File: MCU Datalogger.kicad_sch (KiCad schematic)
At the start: 25 parts, among them U1 DS1337S+, U2 24LC1025, U3 24LC1025, U4 ATMEGA328P-AU, Y1 Crystal, Y2 Crystal

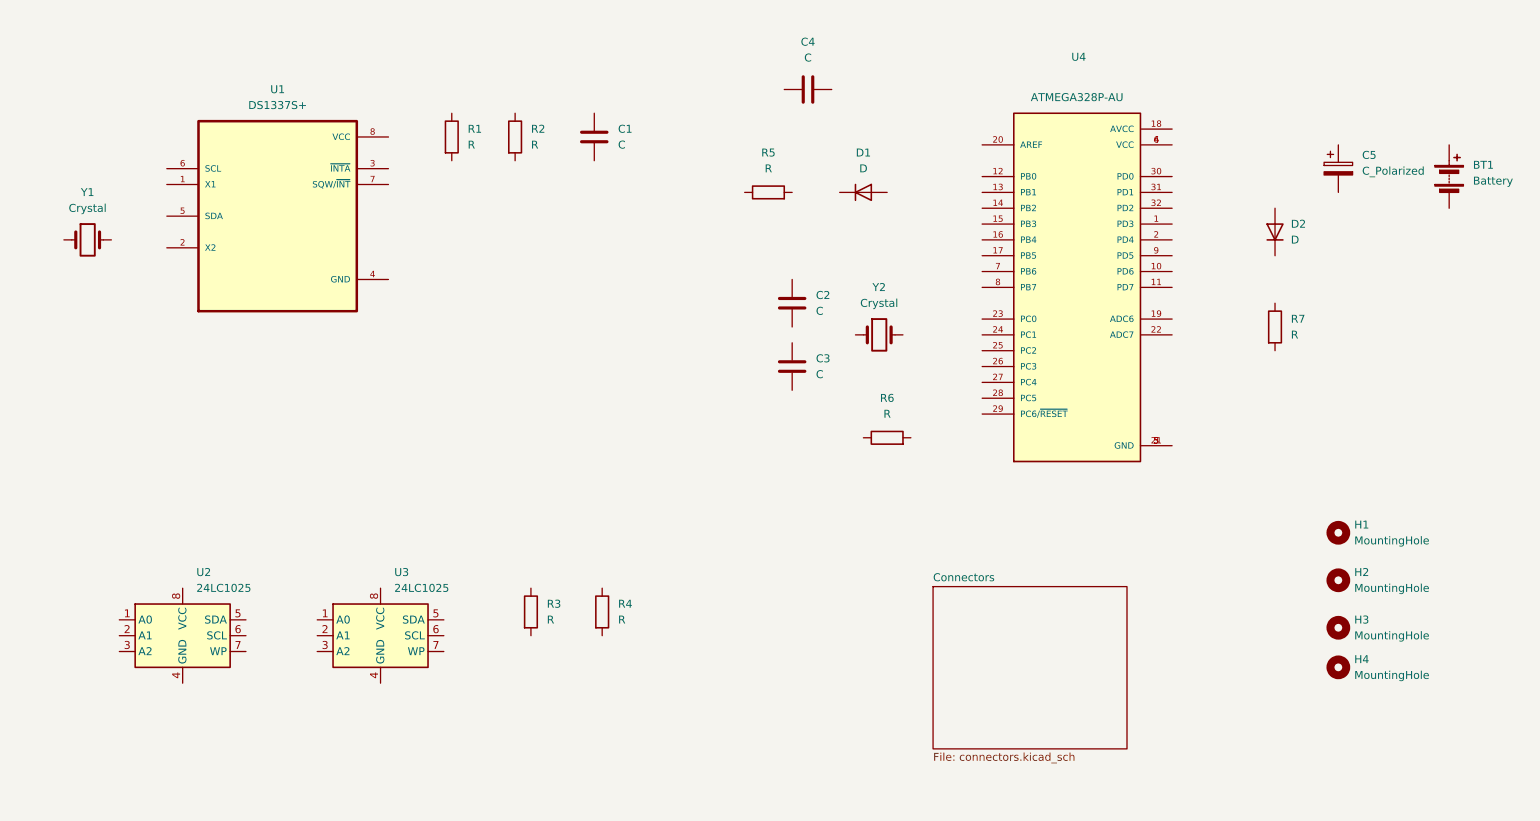
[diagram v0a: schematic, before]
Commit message: Added component values.
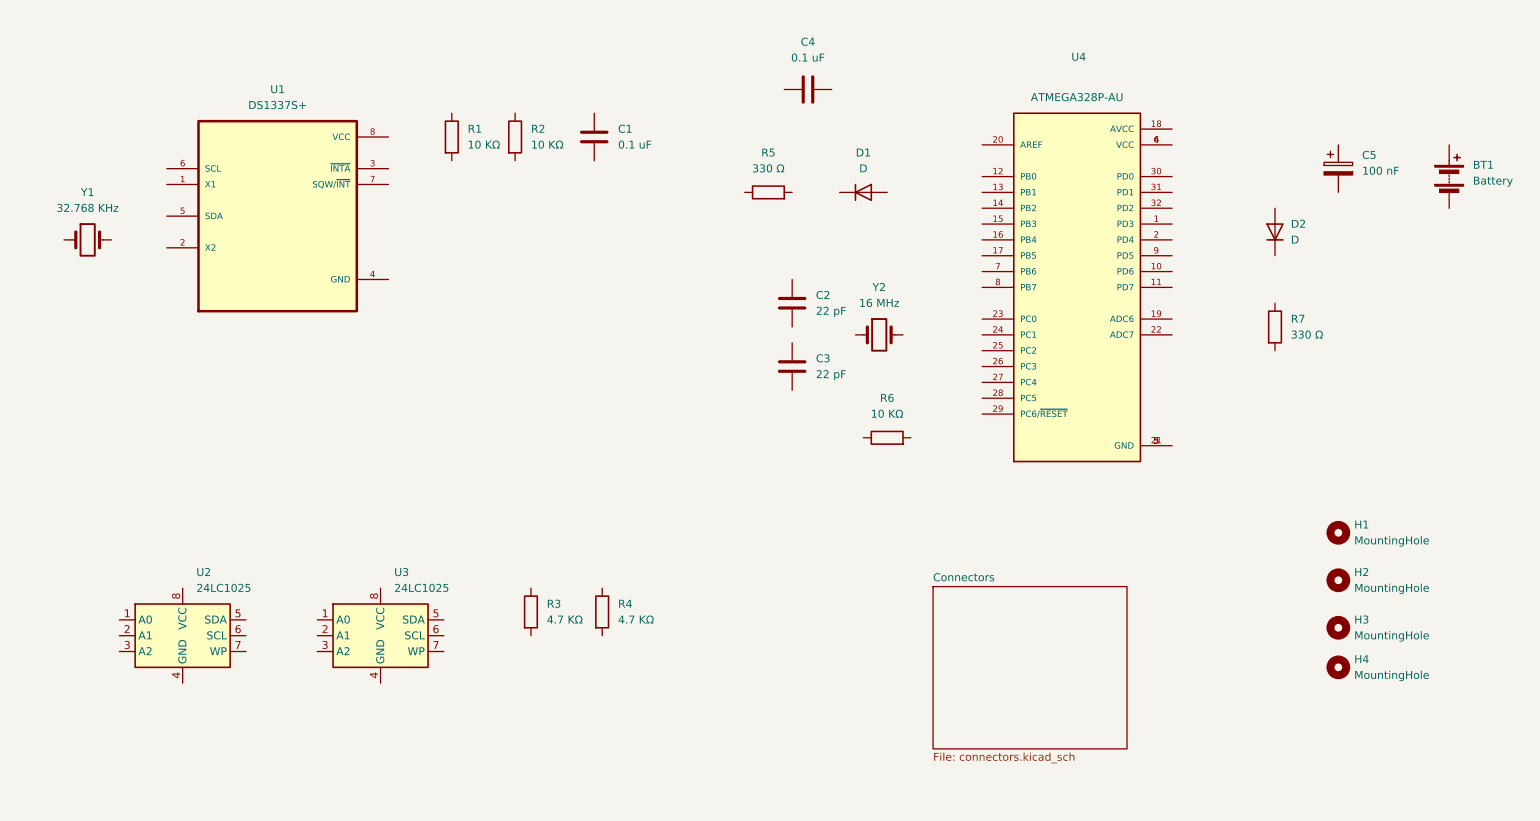
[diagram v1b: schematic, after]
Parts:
- C1, C4: value C -> 0.1 uF
- C2, C3: value C -> 22 pF
- C5: value C_Polarized -> 100 nF
- R1, R2, R6: value R -> 10 ΚΩ
- R3, R4: value R -> 4.7 ΚΩ
- R5, R7: value R -> 330 Ω
- Y1: value Crystal -> 32.768 KHz
- Y2: value Crystal -> 16 MHz
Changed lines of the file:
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@@
 			)
 		)
-		(property "Value" "C"
+		(property "Value" "0.1 uF"
 			(at 146.05 30.48 90)
 			(effects
@@
 			)
 		)
-		(property "Value" "C"
+		(property "Value" "22 pF"
 			(at 147.32 71.1199 0)
 			(effects
@@
 			)
 		)
+		(property "Purpose" ""
+			(at 143.51 69.85 0)
+			(effects
+				(font
+					(size 1.27 1.27)
+				)
+			)
+		)
 		(pin "2"
 		)
@@
 			)
 		)
-		(property "Value" "R"
+		(property "Value" "10 ΚΩ"
 			(at 158.75 87.63 90)
 			(effects
@@
 			)
 		)
-		(property "Value" "C"
+		(property "Value" "0.1 uF"
 			(at 115.57 44.4499 0)
 			(effects
@@
 			)
 		)
-		(property "Value" "R"
+		(property "Value" "10 ΚΩ"
 			(at 101.6 44.4499 0)
 			(effects
@@
 			)
 		)
-		(property "Value" "R"
+		(property "Value" "4.7 ΚΩ"
 			(at 104.14 120.6499 0)
 			(effects
@@
 			)
 		)
-		(property "Value" "R"
+		(property "Value" "10 ΚΩ"
 			(at 91.44 44.4499 0)
 			(effects
@@
 			)
 		)
-		(property "Value" "R"
+		(property "Value" "4.7 ΚΩ"
 			(at 115.57 120.6499 0)
 			(effects
@@
 			)
 		)
-		(property "Value" "Crystal"
+		(property "Value" "32.768 KHz"
 			(at 30.48 54.61 0)
 			(effects
@@
 			)
 		)
-		(property "Value" "Crystal"
+		(property "Value" "16 MHz"
 			(at 157.48 69.85 0)
 			(effects
@@
 			)
 		)
-		(property "Value" "C_Polarized"
+		(property "Value" "100 nF"
 			(at 234.95 48.6409 0)
 			(effects
@@
 			)
 		)
-		(property "Value" "R"
+		(property "Value" "330 Ω"
 			(at 139.7 48.26 90)
 			(effects
@@
 			)
 		)
-		(property "Value" "R"
+		(property "Value" "330 Ω"
 			(at 223.52 74.9299 0)
 			(effects
@@
 			)
 		)
-		(property "Value" "C"
+		(property "Value" "22 pF"
 			(at 147.32 81.2799 0)
 			(effects

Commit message: Completed symbol—footprint associations.
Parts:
- BT1: footprint (none) -> Connector_PinHeader_2.54mm:PinHeader_1x02_P2.54mm_Vertical
- C1, C2, C3, C4, C5: footprint (none) -> Capacitor_SMD:C_0805_2012Metric
- D1, D2: footprint (none) -> LED_SMD:LED_0805_2012Metric
- H1, H2, H3, H4: footprint (none) -> MountingHole:MountingHole_2.1mm
- R1, R2, R3, R4, R5, R6, R7: footprint (none) -> Resistor_SMD:R_0805_2012Metric
- U1: footprint SOIC127P600X175-8N -> Footprints:SOIC127P600X175-8N
- U2, U3: footprint (none) -> Package_SO:SOIC-8_5.23x5.23mm_P1.27mm
- U4: footprint QFP80P900X900X120-32N -> Footprints:QFP80P900X900X120-32N
- Y1, Y2: footprint (none) -> Crystal:Crystal_SMD_5032-2Pin_5.0x3.2mm_HandSoldering
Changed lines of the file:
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@@
 			)
 		)
-		(property "Footprint" ""
+		(property "Footprint" "Capacitor_SMD:C_0805_2012Metric"
 			(at 149.86 34.5948 0)
 			(effects
@@
 			)
 		)
-		(property "Footprint" ""
+		(property "Footprint" "Capacitor_SMD:C_0805_2012Metric"
 			(at 144.4752 73.66 0)
 			(effects
@@
 			)
 		)
-		(property "Footprint" ""
+		(property "Footprint" "Resistor_SMD:R_0805_2012Metric"
 			(at 158.75 93.218 90)
 			(effects
@@
 			)
 		)
-		(property "Footprint" ""
+		(property "Footprint" "Capacitor_SMD:C_0805_2012Metric"
 			(at 112.7252 46.99 0)
 			(effects
@@
 			)
 		)
-		(property "Footprint" ""
+		(property "Footprint" "LED_SMD:LED_0805_2012Metric"
 			(at 220.98 58.42 0)
 			(effects
@@
 			)
 		)
-		(property "Footprint" ""
+		(property "Footprint" "Resistor_SMD:R_0805_2012Metric"
 			(at 97.282 43.18 90)
 			(effects
@@
 			)
 		)
-		(property "Footprint" ""
+		(property "Footprint" "Resistor_SMD:R_0805_2012Metric"
 			(at 99.822 119.38 90)
 			(effects
@@
 			)
 		)
-		(property "Footprint" ""
+		(property "Footprint" "Resistor_SMD:R_0805_2012Metric"
 			(at 87.122 43.18 90)
 			(effects
@@
 			)
 		)
-		(property "Footprint" ""
+		(property "Footprint" "Connector_PinHeader_2.54mm:PinHeader_1x02_P2.54mm_Vertical"
 			(at 248.92 48.006 90)
 			(effects
@@
 			)
 		)
-		(property "Footprint" ""
+		(property "Footprint" "Resistor_SMD:R_0805_2012Metric"
 			(at 111.252 119.38 90)
 			(effects
@@
 			)
 		)
-		(property "Footprint" "QFP80P900X900X120-32N"
+		(property "Footprint" "Footprints:QFP80P900X900X120-32N"
 			(at 189.23 67.31 0)
 			(effects
@@
 			)
 		)
-		(property "Footprint" ""
+		(property "Footprint" "MountingHole:MountingHole_2.1mm"
 			(at 231.14 121.92 0)
 			(effects
@@
 			)
 		)
-		(property "Footprint" ""
+		(property "Footprint" "Crystal:Crystal_SMD_5032-2Pin_5.0x3.2mm_HandSoldering"
 			(at 30.48 59.69 0)
 			(effects
@@
 			)
 		)
-		(property "Footprint" ""
+		(property "Footprint" "MountingHole:MountingHole_2.1mm"
 			(at 231.14 106.68 0)
 			(effects
@@
 			)
 		)
-		(property "Footprint" ""
+		(property "Footprint" "Package_SO:SOIC-8_5.23x5.23mm_P1.27mm"
 			(at 77.47 123.19 0)
 			(effects
@@
 			)
 		)
-		(property "Footprint" "SOIC127P600X175-8N"
+		(property "Footprint" "Footprints:SOIC127P600X175-8N"
 			(at 60.96 55.88 0)
 			(effects
@@
 			)
 		)
-		(property "Footprint" ""
+		(property "Footprint" "MountingHole:MountingHole_2.1mm"
 			(at 231.14 114.3 0)
 			(effects
@@
 			)
 		)
-		(property "Footprint" ""
+		(property "Footprint" "Package_SO:SOIC-8_5.23x5.23mm_P1.27mm"
 			(at 45.72 123.19 0)
 			(effects
@@
 			)
 		)
-		(property "Footprint" ""
+		(property "Footprint" "LED_SMD:LED_0805_2012Metric"
 			(at 154.94 52.07 0)
 			(effects
@@
 			)
 		)
-		(property "Footprint" ""
+		(property "Footprint" "MountingHole:MountingHole_2.1mm"
 			(at 231.14 128.27 0)
 			(effects
@@
 			)
 		)
-		(property "Footprint" ""
+		(property "Footprint" "Crystal:Crystal_SMD_5032-2Pin_5.0x3.2mm_HandSoldering"
 			(at 157.48 74.93 0)
 			(effects
@@
 			)
 		)
-		(property "Footprint" ""
+		(property "Footprint" "Capacitor_SMD:C_0805_2012Metric"
 			(at 232.1052 52.07 0)
 			(effects
@@
 			)
 		)
-		(property "Footprint" ""
+		(property "Footprint" "Resistor_SMD:R_0805_2012Metric"
 			(at 139.7 53.848 90)
 			(effects
@@
 			)
 		)
-		(property "Footprint" ""
+		(property "Footprint" "Resistor_SMD:R_0805_2012Metric"
 			(at 219.202 73.66 90)
 			(effects
@@
 			)
 		)
-		(property "Footprint" ""
+		(property "Footprint" "Capacitor_SMD:C_0805_2012Metric"
 			(at 144.4752 83.82 0)
 			(effects

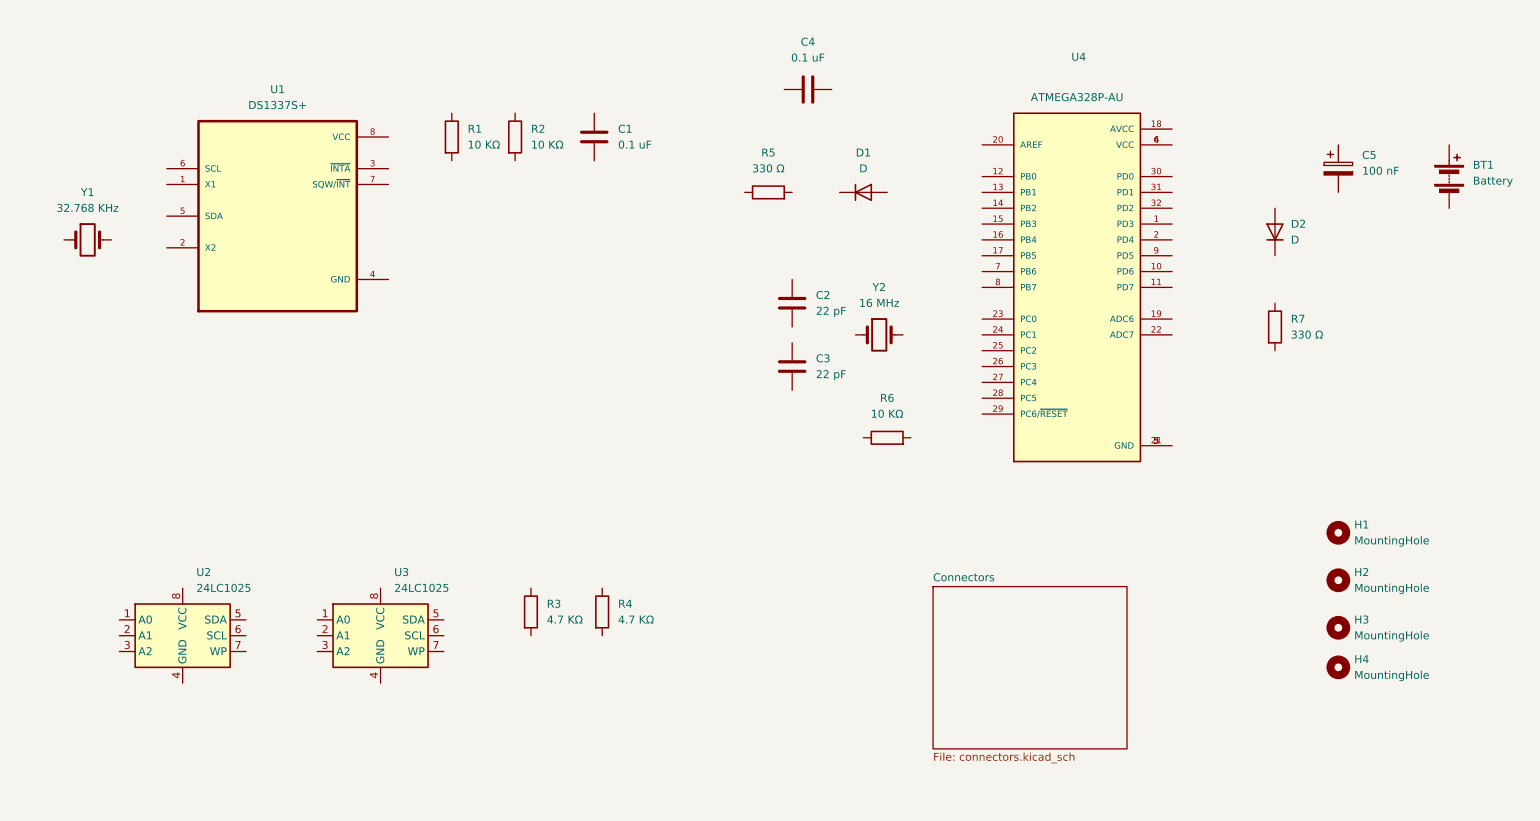
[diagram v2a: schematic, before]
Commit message: Completed wiring of main sheet.
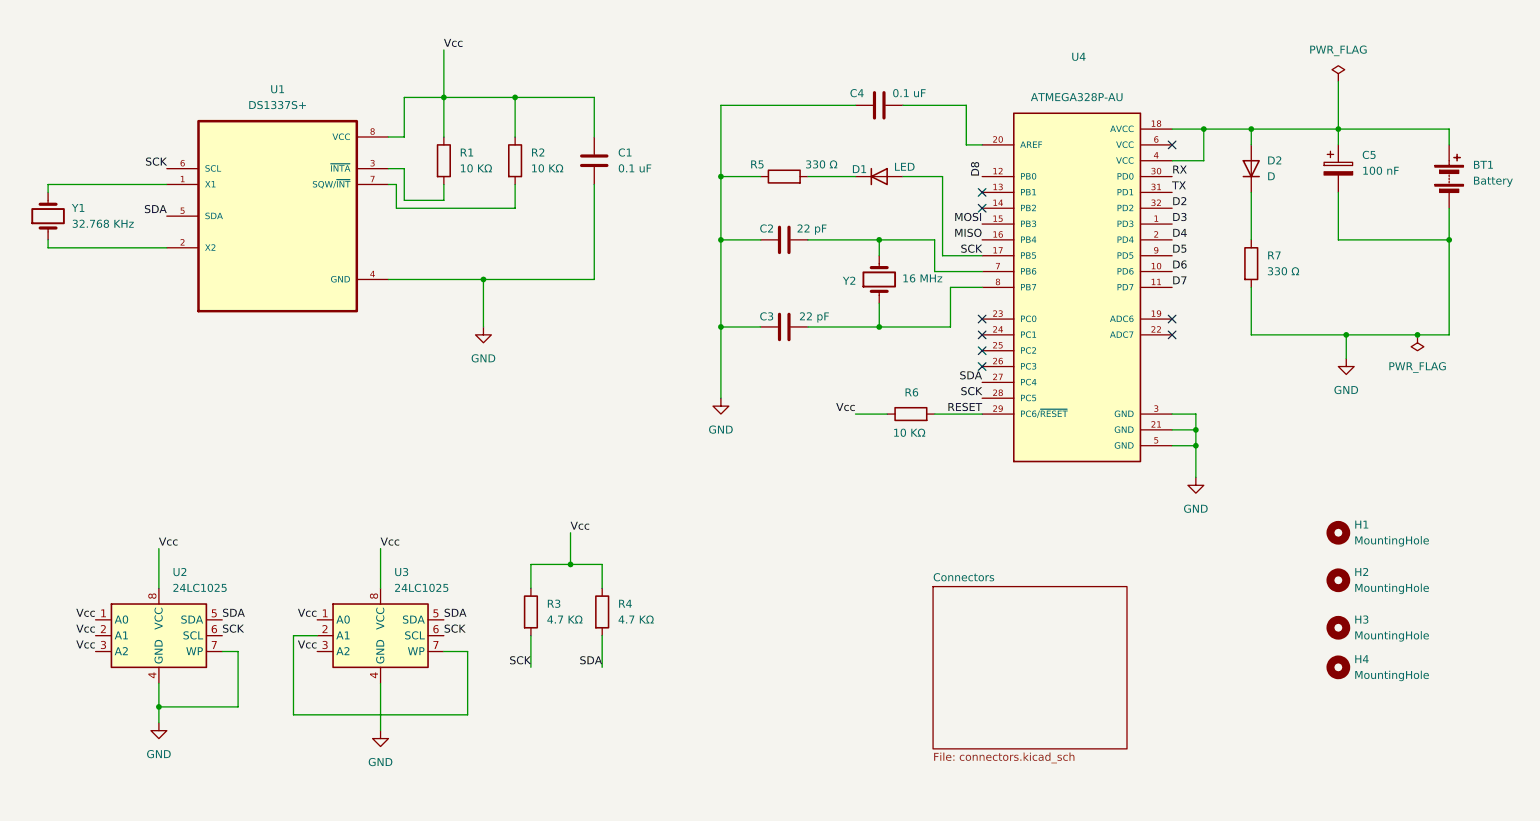
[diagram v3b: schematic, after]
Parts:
- D1: value D -> LED
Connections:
- net GND: now reaches C4.1
- net GND: now also BT1.2 (-), C1.2, C2.2, C3.1, C5.2, R5.1, R7.2, U1.4 (GND), U2.4 (GND), U2.7 (WP), U3.4 (GND), U4.21 (GND), U4.3 (GND), U4.5 (GND)
- net at C4.2: now also U4.20 (AREF)
- net at C2.1: now also U4.7 (PB6), Y2.2
- net Vcc: now reaches R6.1
- net Vcc: now also C1.1, R1.1, R2.1, R3.1, R4.1, U1.8 (VCC), U2.1 (A0), U2.2 (A1), U2.3 (A2), U2.8 (VCC), U3.1 (A0), U3.3 (A2), U3.8 (VCC)
- net RESET: now reaches R6.2
- net RESET: now also U4.29 (PC6/~{RESET})
- net at D2.1 (K): now also R7.1
- net at D2.2 (A): now also BT1.1 (+), C5.1, U4.18 (AVCC), U4.4 (VCC)
- net at R2.2: now also U1.7 (SQW/~{INT})
- net SCK: now reaches R3.2
- net SCK: now also D1.2 (A), U1.6 (SCL), U2.6 (SCL), U3.6 (SCL), U4.17 (PB5), U4.28 (PC5)
- net at R1.2: now also U1.3 (~{INTA})
- net SDA: now reaches R4.2
- net SDA: now also U1.5 (SDA), U2.5 (SDA), U3.5 (SDA), U4.27 (PC4)
- net D3: now reaches U4.1 (PD3)
- net D6: now reaches U4.10 (PD6)
- net D7: now reaches U4.11 (PD7)
- net D8: now reaches U4.12 (PB0)
- net MOSI: now reaches U4.15 (PB3)
- net MISO: now reaches U4.16 (PB4)
- net D4: now reaches U4.2 (PD4)
- net RX: now reaches U4.30 (PD0)
- net TX: now reaches U4.31 (PD1)
- net D2: now reaches U4.32 (PD2)
- net at U4.6 (VCC): no longer U4.4 (VCC)
- net at U4.8 (PB7): now also C3.2, Y2.1
- net D5: now reaches U4.9 (PD5)
- net at Y1.1: now also U1.2 (X2)
- net at Y1.2: now also U1.1 (X1)
- net at U3.2 (A1): now also U3.7 (WP)
- net at D1.1 (K): now also R5.2
- no-connect marks 0 -> 9
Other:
- moved on the sheet: C1, C2, C3, C4, D1, D2, R1, R2, R5, R6, R7, U2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

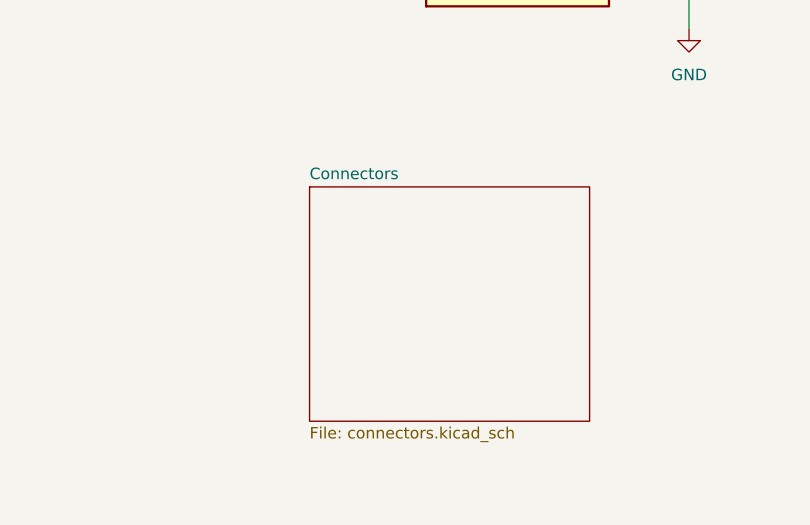
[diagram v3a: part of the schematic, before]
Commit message: Allocated GND and Vcc nets to the Power net class.
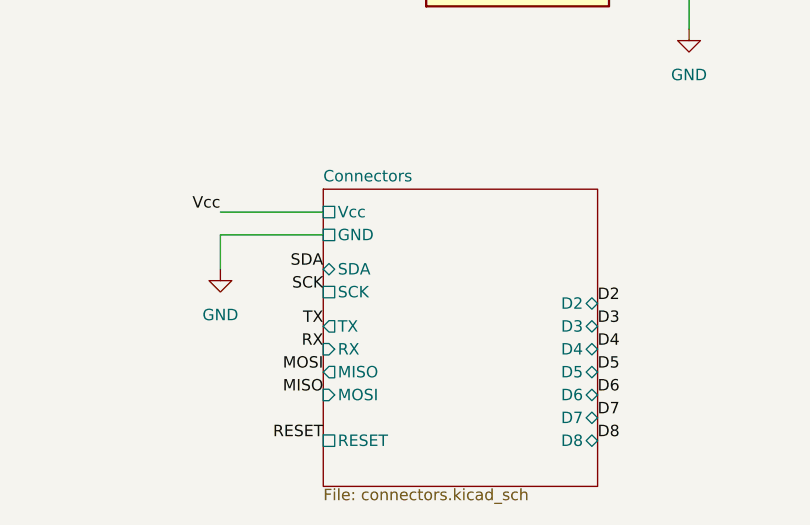
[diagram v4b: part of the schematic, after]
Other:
- sheet Connectors ports: added D2, D3, D4, D5, D6, D7, D8, GND, MISO, MOSI, RESET, RX, SCK, SDA, TX, Vcc; removed none
